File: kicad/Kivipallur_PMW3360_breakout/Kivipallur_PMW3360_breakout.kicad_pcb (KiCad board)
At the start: 2 copper layers, 22 x 25 mm, 10 parts, among them J1 Conn_01x07, U1 LP2985-1.8, U2 PMW3360DM-T2QU

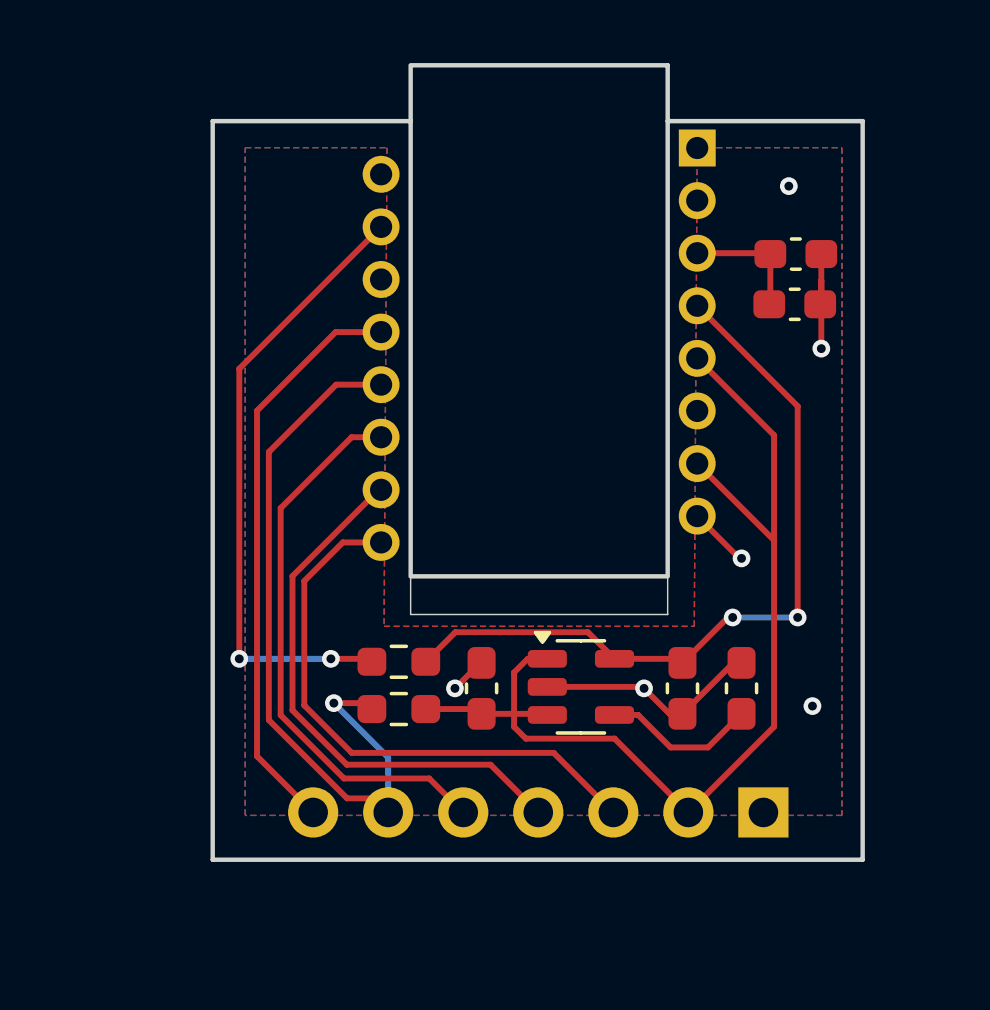
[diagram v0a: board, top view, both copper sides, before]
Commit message: Change PMW3360 footprint outline, finalize others
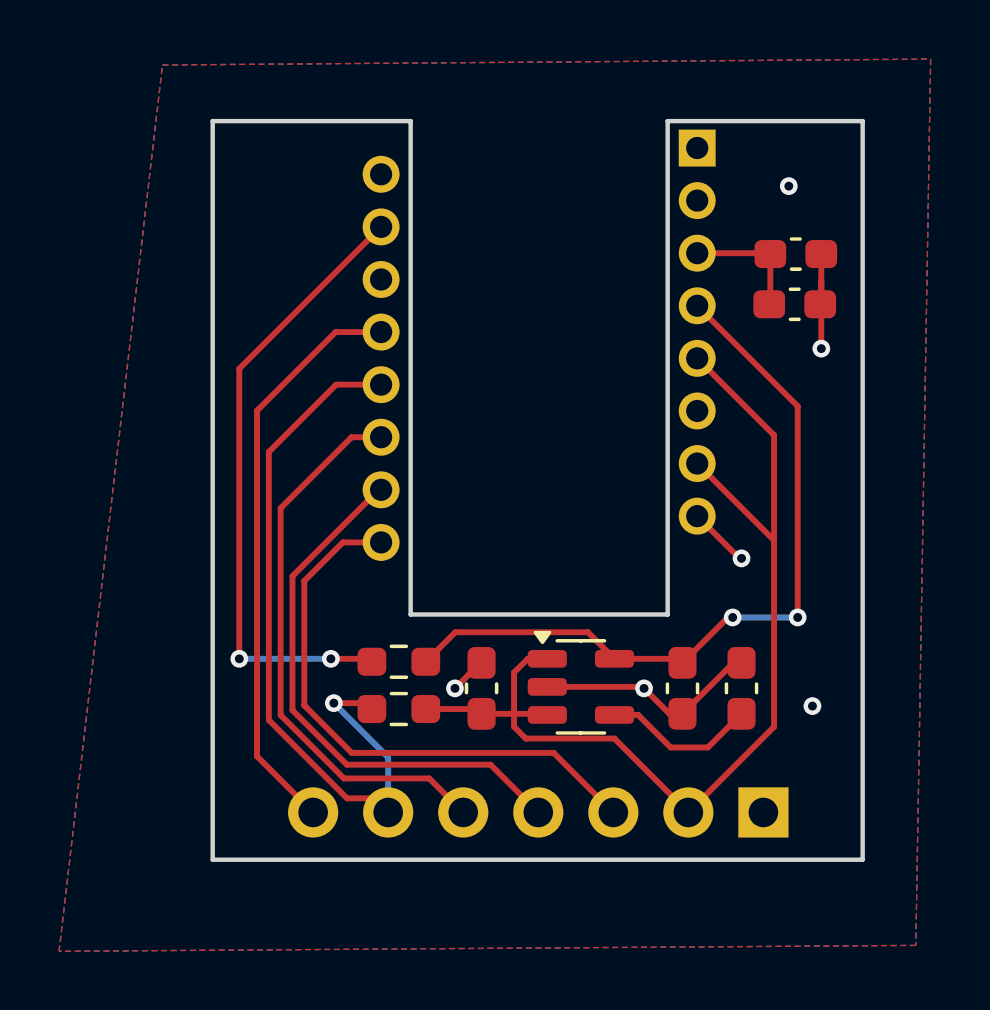
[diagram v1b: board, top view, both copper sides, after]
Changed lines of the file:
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@@
 			(plot_on_all_layers_selection 0x0000000_00000000)
 			(disableapertmacros no)
-			(usegerberextensions no)
-			(usegerberattributes yes)
-			(usegerberadvancedattributes yes)
-			(creategerberjobfile yes)
+			(usegerberextensions yes)
+			(usegerberattributes no)
+			(usegerberadvancedattributes no)
+			(creategerberjobfile no)
 			(dashed_line_dash_ratio 12.000000)
 			(dashed_line_gap_ratio 3.000000)
@@
 			(psa4output no)
 			(plotreference yes)
-			(plotvalue yes)
+			(plotvalue no)
 			(plotfptext yes)
 			(plotinvisibletext no)
 			(sketchpadsonfab no)
-			(subtractmaskfromsilk no)
+			(subtractmaskfromsilk yes)
 			(outputformat 1)
 			(mirror no)
-			(drillshape 1)
+			(drillshape 0)
 			(scaleselection 1)
-			(outputdirectory "")
+			(outputdirectory "../../gerbers/Kivipallur_PMW3360_breakout/")
 		)
 	)
@@
 		)
 		(fp_rect
-			(start -8.968 -4.35)
-			(end 8.332 4.35)
-			(stroke
-				(width 0.15)
-				(type solid)
-			)
-			(fill none)
-			(layer "Edge.Cuts")
-		)
-		(fp_rect
 			(start -9.906 6.604)
 			(end 9.652 -6.604)
@@
 			(at 0 2.33 90)
 			(layer "B.SilkS")
+			(hide yes)
 			(effects
 				(font
@@
 		(end 106.7 66.7)
 		(stroke
-			(width 0.05)
+			(width 0.15)
 			(type default)
 		)
@@
 		(end 115.4 50)
 		(stroke
-			(width 0.05)
+			(width 0.15)
 			(type default)
 		)
@@
 		(end 115.4 66.7)
 		(stroke
-			(width 0.05)
+			(width 0.15)
 			(type default)
 		)
@@
 		(polygon
 			(pts
-				(xy 116.4 50.9) (xy 121.3 50.9) (xy 121.3 73.5) (xy 101.1 73.5) (xy 101.1 50.9) (xy 105.9 50.9)
-				(xy 105.8 67.1) (xy 116.3 67.1)
+				(xy 98.3 48.1) (xy 124.3 47.9) (xy 123.8 77.9) (xy 94.8 78.1)
 			)
 		)
